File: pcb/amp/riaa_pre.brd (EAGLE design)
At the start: 53.3 x 44.5 mm, 43 parts, among them IC1 OPA2134, IC2 OPA2134, X1 22-23-2031

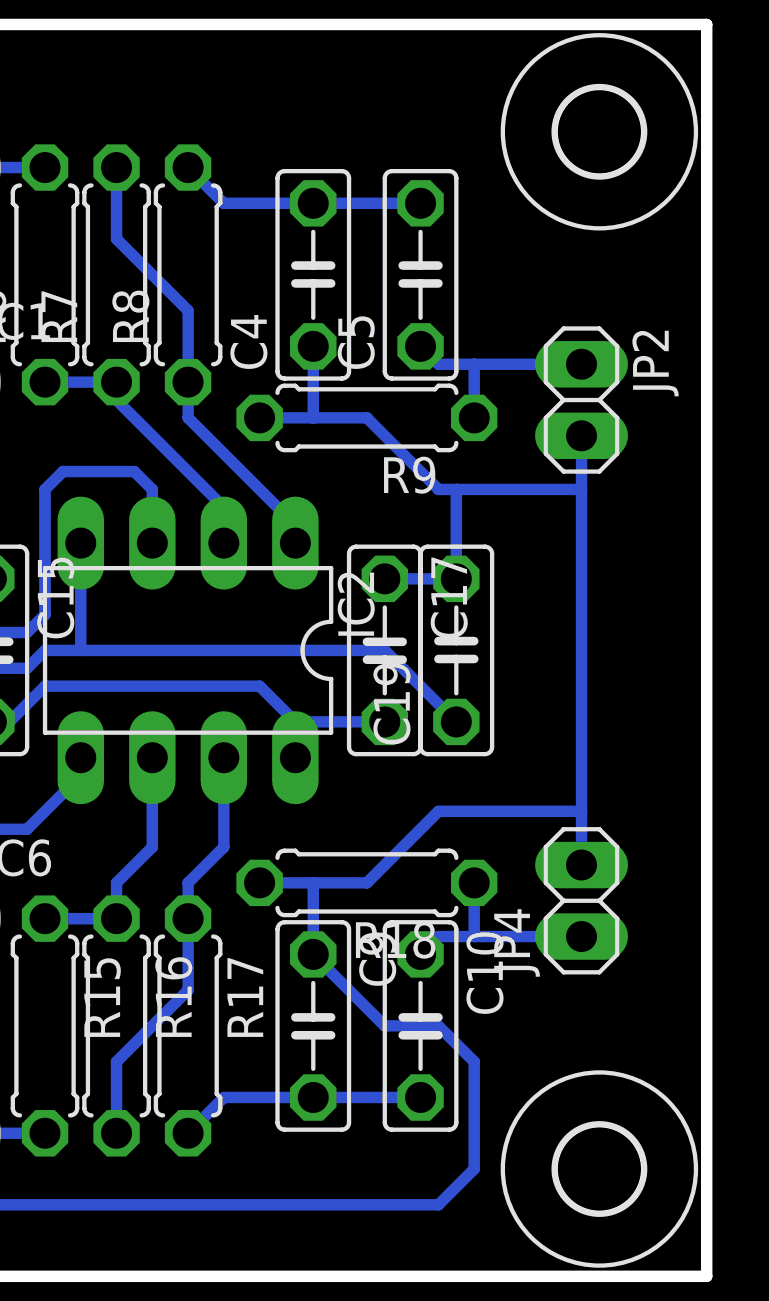
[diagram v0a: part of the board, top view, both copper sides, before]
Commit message: 
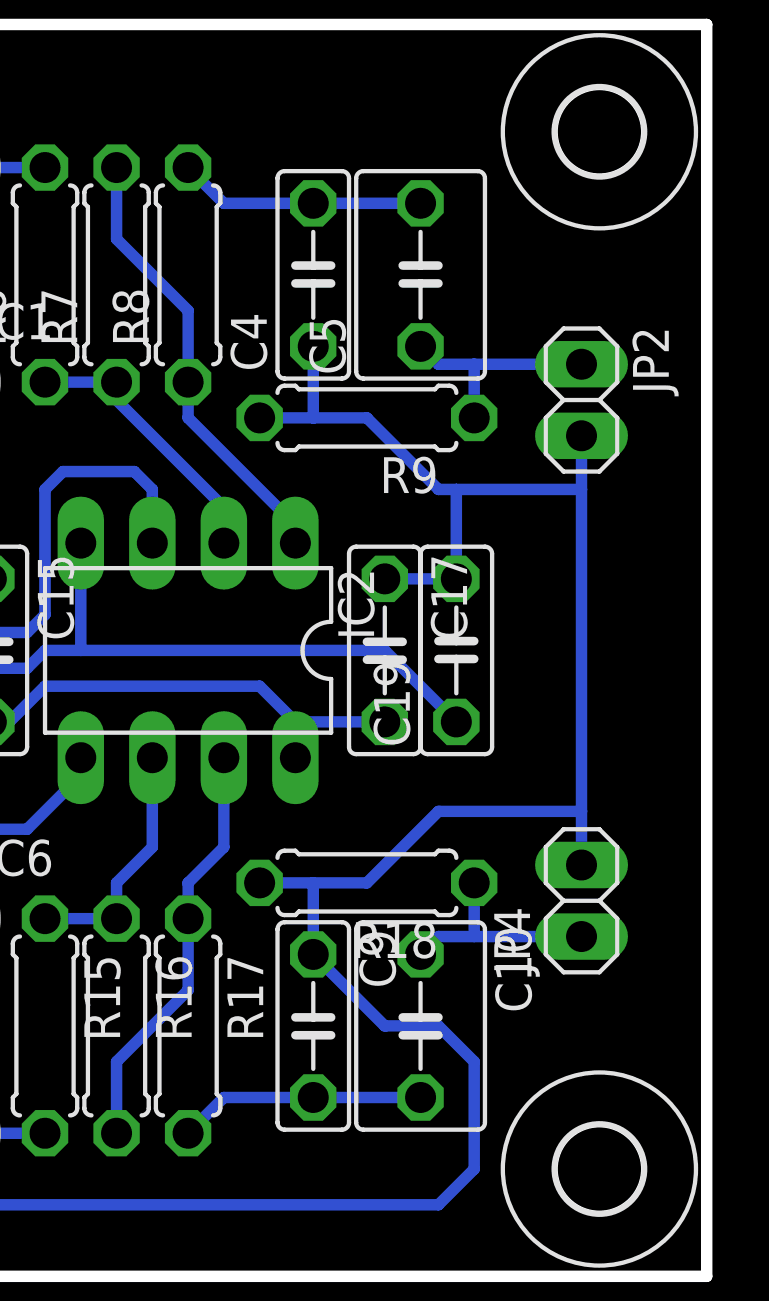
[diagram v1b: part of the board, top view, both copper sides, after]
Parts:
- C10, C5: device amp:C050-025X075 -> amp:C050-045X075
